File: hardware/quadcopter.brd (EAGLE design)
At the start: 130.1 x 130.1 mm, 91 parts, among them J1 HEADER-4POS-0.1IN-FEMALE-SMD-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, J2 HEADER-10POSTH-254X10, J3 HEADER-4POS-0.1IN-FEMALE, J4 AVR_SPI_PRG_6-SMD, M1 MOTOR_PADS_GND-MOLEX-SMD, M2 MOTOR_PADS_GND-MOLEX-SMD, M3 MOTOR_PADS_GND-MOLEX-SMD, M4 MOTOR_PADS_GND-MOLEX-SMD, P1 PROPELLOR-45MM, P2 PROPELLOR-45MM, P3 PROPELLOR-45MM, P4 PROPELLOR-45MM, Q1 N-MOSFET-SI2302DS, Q12 N-MOSFET-SI2302DS, Q2 N-MOSFET-SI2302DS, Q3 N-MOSFET-SI2302DS, Q4 N-MOSFET-SI2302DS, Q6 N-MOSFET-SI2302DS, Q8 N-MOSFET-SI2302DS, Q9 N-MOSFET-SI2302DS, SW1 PUSHBUTTON_-4.5X4.5, U1 ATMEGA128RFA1, U2 IMU_LSM9DS1-LSM9DS1, Y1 CRYSTAL5X3

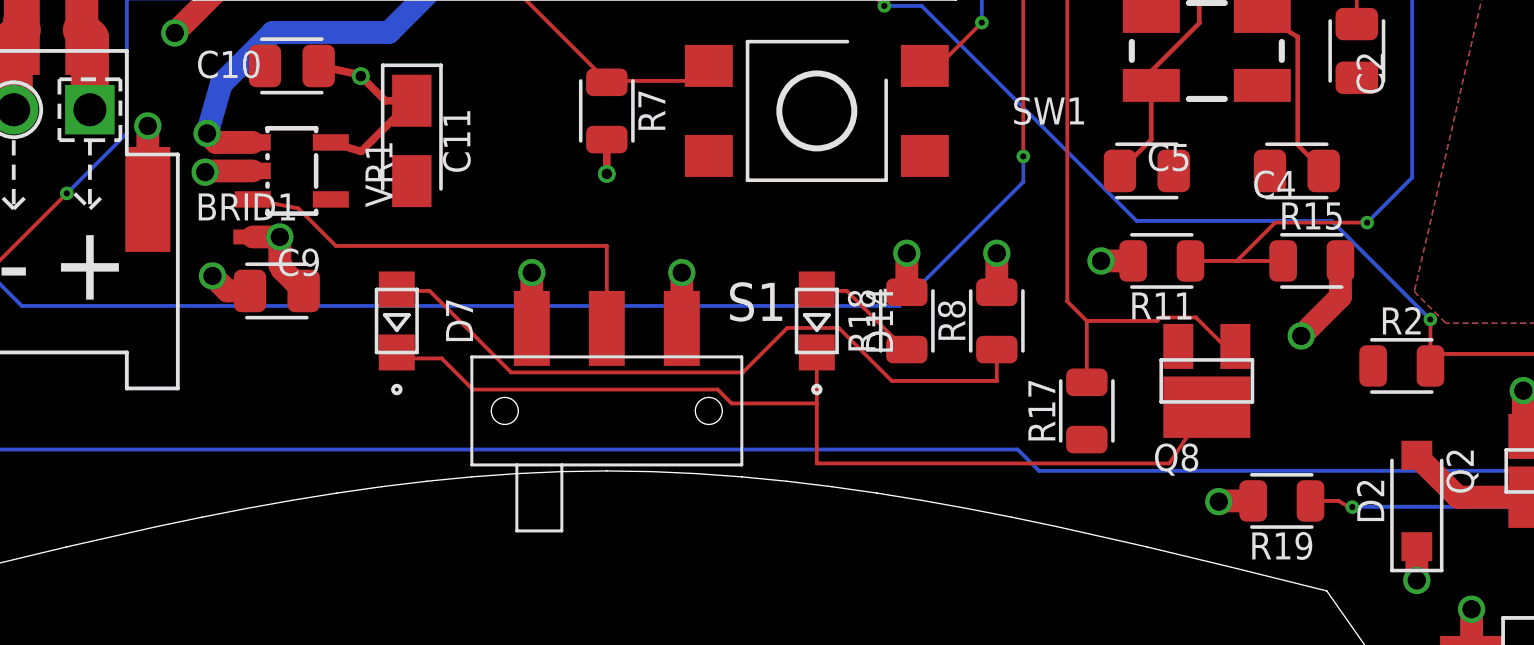
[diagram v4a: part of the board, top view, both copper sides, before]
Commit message: Aligned net bridge to 0.5mm grid
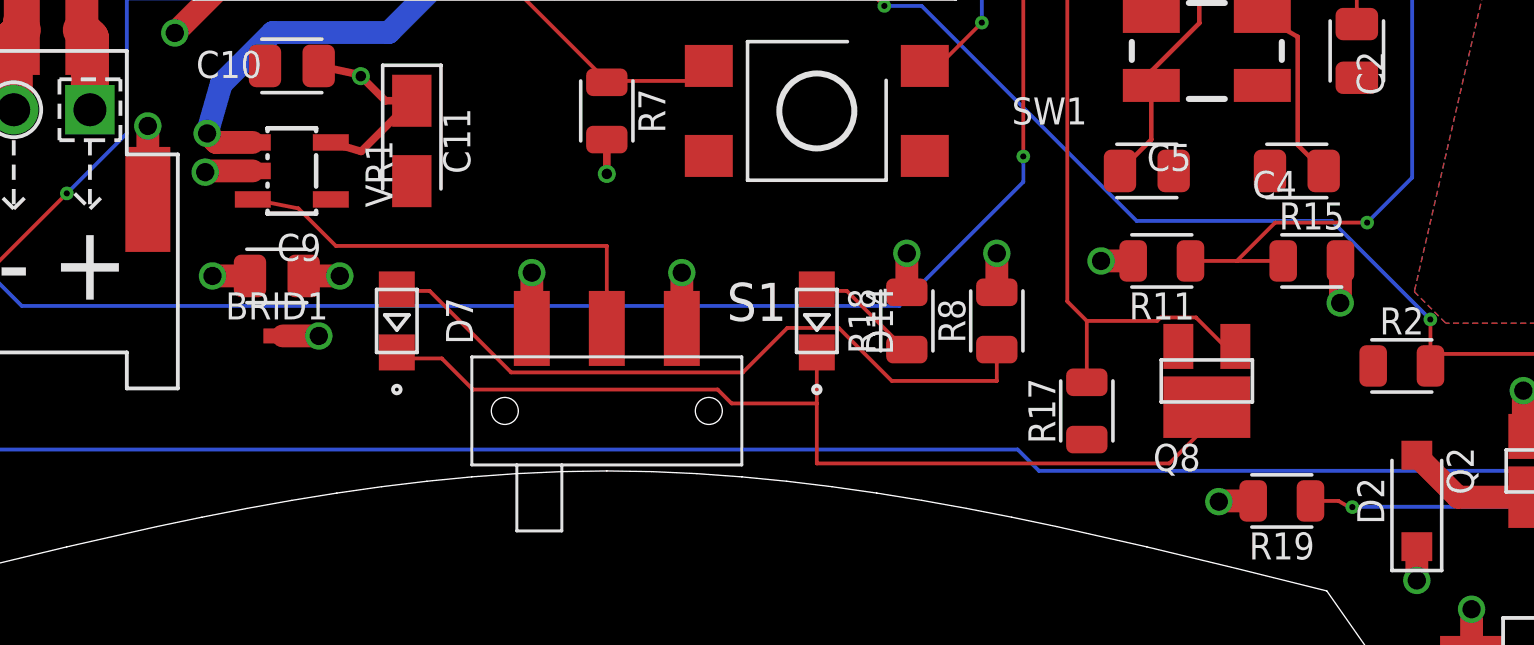
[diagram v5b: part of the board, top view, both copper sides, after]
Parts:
- moved BRID1 3.45 mm to (-11.0, -17.5)
- moved C9 0.50 mm to (-11.0, -15.5)
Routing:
- net BAT_GND: track 50.5 -> 48.2 mm, vias 21 -> 22
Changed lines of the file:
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@@
 <attribute name="NAME" x="-18.5" y="-4.5" size="0.9" layer="25" font="vector" align="center"/>
 </element>
-<element name="BRID1" library="custom_michael_shao" library_urn="urn:adsk.wipprod:fs.file:vf.WEX53KctTd223gU3vuBSuw" package="NET_BRIDGE_5X5" value="NET_BRIDGE_5X5" x="-12" y="-14.2" smashed="yes" rot="R180">
-<attribute name="CREATOR" value="Michael Shao" x="-37.4" y="83.59" size="1.778" layer="27" rot="R180" display="off"/>
-<attribute name="DIST" value="N/A" x="-37.4" y="83.59" size="1.778" layer="27" rot="R180" display="off"/>
-<attribute name="DISTPN" value="N/A" x="-37.4" y="83.59" size="1.778" layer="27" rot="R180" display="off"/>
-<attribute name="NAME" x="-12" y="-13.2" size="0.9" layer="25" font="vector" rot="R180" align="center"/>
+<element name="BRID1" library="custom_michael_shao" library_urn="urn:adsk.wipprod:fs.file:vf.WEX53KctTd223gU3vuBSuw" package="NET_BRIDGE_5X5" value="NET_BRIDGE_5X5" x="-11" y="-17.5" smashed="yes" rot="R180">
+<attribute name="CREATOR" value="Michael Shao" x="-36.4" y="80.29" size="1.778" layer="27" rot="R180" display="off"/>
+<attribute name="DIST" value="N/A" x="-36.4" y="80.29" size="1.778" layer="27" rot="R180" display="off"/>
+<attribute name="DISTPN" value="N/A" x="-36.4" y="80.29" size="1.778" layer="27" rot="R180" display="off"/>
+<attribute name="NAME" x="-11" y="-16.5" size="0.9" layer="25" font="vector" rot="R180" align="center"/>
 </element>
 <element name="C1" library="quadparts_prebuilt_2022" library_urn="urn:adsk.wipprod:fs.file:vf.VudH_-qgS-enOFMGlZoxrw" package="CAPC2012X140_HS" value="22pF" x="28" y="6.5" smashed="yes" rot="R270">
@@
 <attribute name="VALUE" x="20" y="11" size="0.9" layer="27" font="vector" rot="R90"/>
 </element>
-<element name="C9" library="quadparts_prebuilt_2022" library_urn="urn:adsk.wipprod:fs.file:vf.VudH_-qgS-enOFMGlZoxrw" package="CAPC2012X140_HS" value="1uF" x="-11" y="-16" smashed="yes">
-<attribute name="CREATOR" value="Swanson" x="4.24" y="-113.79" size="1.778" layer="27" display="off"/>
-<attribute name="DIST" value="Digikey" x="4.24" y="-113.79" size="1.778" layer="27" display="off"/>
-<attribute name="DISTPN" value="587-1281-1-ND" x="4.24" y="-113.79" size="1.778" layer="27" display="off"/>
-<attribute name="MFR" value="Taiyo Yuden" x="4.24" y="-113.79" size="1.778" layer="27" display="off"/>
-<attribute name="MOUNTING" value="SMD" x="4.24" y="-113.79" size="1.778" layer="27" display="off"/>
-<attribute name="MPN" value="TMK212B7105KG-T" x="4.24" y="-113.79" size="1.778" layer="27" display="off"/>
-<attribute name="NAME" x="-11" y="-15.5" size="0.9" layer="25" font="vector"/>
-<attribute name="REVIEWER" value="Swanson" x="4.24" y="-113.79" size="1.778" layer="27" display="off"/>
-<attribute name="VALUE" x="-10" y="-18" size="0.9" layer="27" font="vector"/>
+<element name="C9" library="quadparts_prebuilt_2022" library_urn="urn:adsk.wipprod:fs.file:vf.VudH_-qgS-enOFMGlZoxrw" package="CAPC2012X140_HS" value="1uF" x="-11" y="-15.5" smashed="yes">
+<attribute name="CREATOR" value="Swanson" x="4.24" y="-113.29" size="1.778" layer="27" display="off"/>
+<attribute name="DIST" value="Digikey" x="4.24" y="-113.29" size="1.778" layer="27" display="off"/>
+<attribute name="DISTPN" value="587-1281-1-ND" x="4.24" y="-113.29" size="1.778" layer="27" display="off"/>
+<attribute name="MFR" value="Taiyo Yuden" x="4.24" y="-113.29" size="1.778" layer="27" display="off"/>
+<attribute name="MOUNTING" value="SMD" x="4.24" y="-113.29" size="1.778" layer="27" display="off"/>
+<attribute name="MPN" value="TMK212B7105KG-T" x="4.24" y="-113.29" size="1.778" layer="27" display="off"/>
+<attribute name="NAME" x="-11" y="-15" size="0.9" layer="25" font="vector"/>
+<attribute name="REVIEWER" value="Swanson" x="4.24" y="-113.29" size="1.778" layer="27" display="off"/>
+<attribute name="VALUE" x="-10" y="-17.5" size="0.9" layer="27" font="vector"/>
 </element>
 <element name="D1" library="quadparts_prebuilt_2022" library_urn="urn:adsk.wipprod:fs.file:vf.VudH_-qgS-enOFMGlZoxrw" package="SODFL3516X96" package3d_urn="urn:adsk.eagle:package:11793366/1" value="360mV" x="32" y="22.5" smashed="yes" rot="R180">
@@
 <vertex x="14.98484375" y="14.0762"/>
 </polygon>
-<via x="23.1454" y="-17.5" extent="1-16" drill="0.6096"/>
+<via x="24.4454" y="-16.4" extent="1-16" drill="0.6096"/>
 <wire x1="-12.5" y1="-5" x2="-12.5" y2="-5.5" width="0.762" layer="1"/>
 <wire x1="-12.5" y1="-5.5" x2="-14.4" y2="-7.4" width="0.762" layer="1"/>
@@
 <wire x1="-21.7" y1="-12.95" x2="-21.7" y2="-10.5" width="0.762" layer="1"/>
 <via x="-21.7" y="-10.5" extent="1-16" drill="0.6096"/>
-<wire x1="24.455" y1="-15" x2="24.455" y2="-16.1904" width="0.762" layer="1"/>
-<wire x1="24.455" y1="-16.1904" x2="23.1454" y2="-17.5" width="0.762" layer="1"/>
+<wire x1="24.455" y1="-15" x2="24.455" y2="-16.3904" width="0.762" layer="1"/>
+<wire x1="24.455" y1="-16.3904" x2="24.4454" y2="-16.4" width="0.762" layer="1"/>
 <wire x1="-19.77" y1="-9.96" x2="-19.77" y2="-7.57" width="1.27" layer="1"/>
 <wire x1="-19.77" y1="-7.57" x2="-19.5" y2="-7.3" width="1.27" layer="1"/>
@@
 <wire x1="-13.3877125" y1="-12.0406" x2="-13.3471125" y2="-12" width="0.762" layer="1"/>
 <wire x1="-13.3471125" y1="-12" x2="-11.8" y2="-12" width="0.762" layer="1"/>
-<wire x1="-11.8" y1="-14.2" x2="-10.9" y2="-14.2" width="0.762" layer="1"/>
-<via x="-10.9" y="-14.2" extent="1-16" drill="0.6096"/>
-<wire x1="-10.105" y1="-16" x2="-10.8216" y2="-15.2834" width="0.762" layer="1"/>
-<wire x1="-10.8216" y1="-15.2834" x2="-10.8216" y2="-15.21456875" width="0.762" layer="1"/>
-<wire x1="-10.8216" y1="-15.21456875" x2="-10.9" y2="-15.13616875" width="0.762" layer="1"/>
-<wire x1="-10.9" y1="-15.13616875" x2="-10.9" y2="-14.2" width="0.762" layer="1"/>
+<via x="-9.6" y="-17.5" extent="1-16" drill="0.6096"/>
+<wire x1="-8.9" y1="-15.5" x2="-10.105" y2="-15.5" width="0.762" layer="1"/>
+<via x="-8.9" y="-15.5" extent="1-16" drill="0.6096"/>
+<wire x1="-10.8" y1="-17.5" x2="-9.6" y2="-17.5" width="0.762" layer="1"/>
 </signal>
 <signal name="VBAT" class="3">
@@
 <wire x1="-11.8" y1="-11.05" x2="-13.0245" y2="-11.05" width="0.762" layer="1"/>
 <wire x1="-13.0245" y1="-11.05" x2="-13.3245" y2="-10.75" width="0.762" layer="1"/>
-<wire x1="-11.895" y1="-16" x2="-12.6446" y2="-16" width="0.762" layer="1"/>
-<wire x1="-12.6446" y1="-16" x2="-13.1446" y2="-15.5" width="0.762" layer="1"/>
+<wire x1="-11.895" y1="-15.5" x2="-13.1446" y2="-15.5" width="0.762" layer="1"/>
 </signal>
 <signal name="N$1" class="3">
@@
 <wire x1="3.69554375" y1="-19.2865" x2="-4.4635" y2="-19.2865" width="0.127" layer="1"/>
 <wire x1="7" y1="-21.75" x2="18.75" y2="-21.75" width="0.127" layer="1"/>
-<wire x1="18.75" y1="-21.75" x2="20" y2="-19.875" width="0.127" layer="1"/>
+<wire x1="20" y1="-19.875" x2="20" y2="-20.5" width="0.127" layer="1"/>
+<wire x1="20" y1="-20.5" x2="18.75" y2="-21.75" width="0.127" layer="1"/>
 </signal>
 <signal name="N$28">

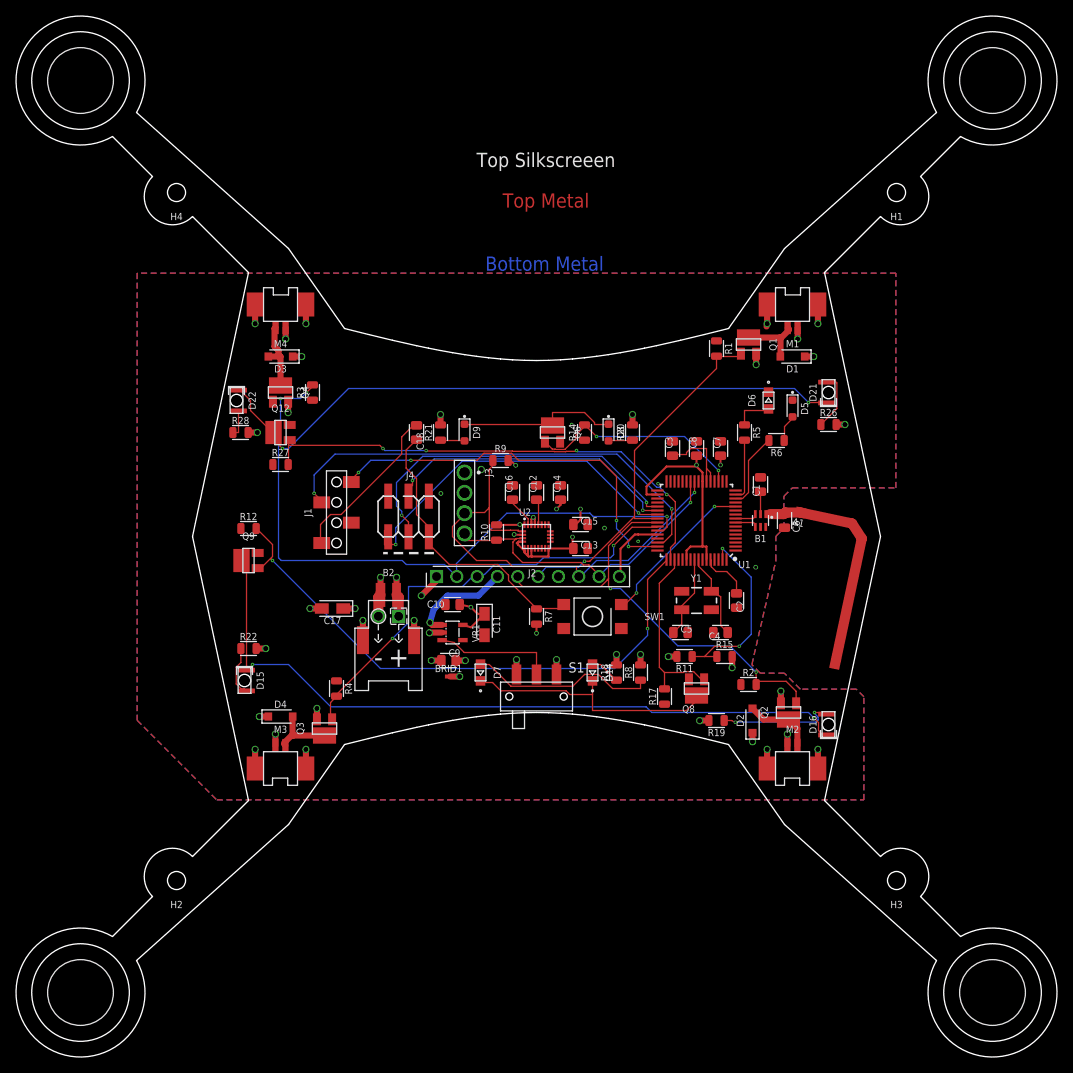
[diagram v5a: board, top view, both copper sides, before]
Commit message: Fixed issues identified in human review
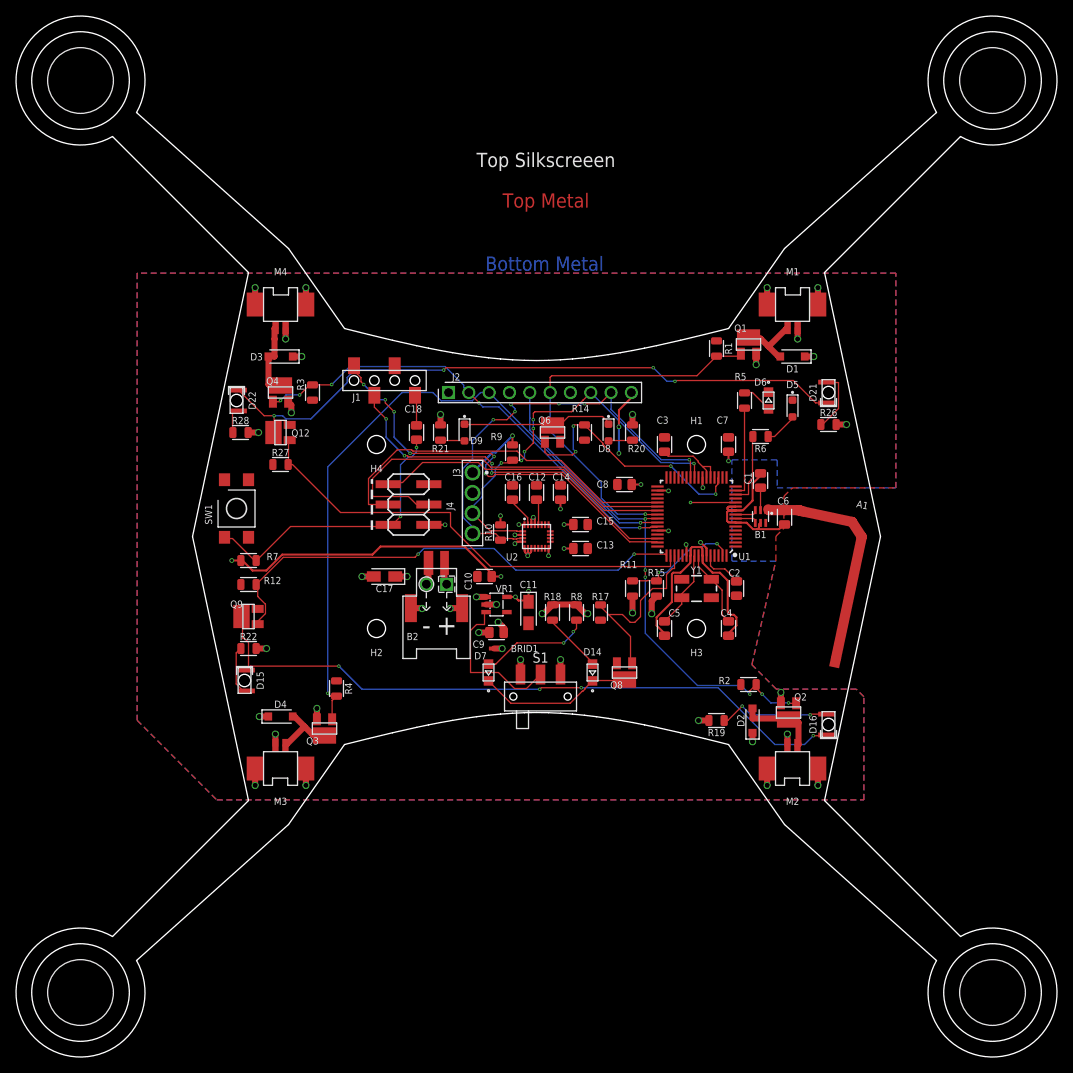
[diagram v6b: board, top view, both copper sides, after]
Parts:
- moved SW1 46.5 mm to (-37.5, 3.50), turned to 270 degrees
- moved H1 40.2 mm to (20.0, 11.5)
- moved H2 40.2 mm to (-20.0, -11.5)
- moved H3 40.2 mm to (20.0, -11.5)
- moved H4 40.2 mm to (-20.0, 11.5)
- moved R7 36.7 mm to (-36.0, -3.00), turned to 180 degrees
- moved J2 23.0 mm to (-11.0, 18.0)
- moved J1 17.6 mm to (-19.0, 19.5), turned to 180 degrees
- moved R17 13.2 mm to (8.00, -9.50)
- moved R15 12.0 mm to (15.0, -6.50), turned to 270 degrees
- moved R18 11.0 mm to (2.00, -9.50)
- moved R8 11.0 mm to (5.00, -9.50)
- moved R11 10.7 mm to (12.0, -6.50), turned to 270 degrees
- moved C8 10.1 mm to (11.0, 6.50), turned to 180 degrees
- moved Q8 9.22 mm to (11.0, -17.0)
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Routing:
- net GND: track 0.00 -> 50.8 mm, vias 7 -> 1
- net PWM3: track 55.7 -> 85.4 mm
- net PWM4: track 82.8 -> 58.5 mm, vias 3 -> 5
- net RESET: track 57.1 -> 79.5 mm, vias 2 -> 3
- net SDA: track 40.2 -> 57.3 mm, vias 1 -> 6
- net N$6: track 20.8 -> 3.85 mm
- net N$27: track 32.7 -> 19.5 mm
- net RX0: track 57.8 -> 45.8 mm, vias 2 -> 4
- net MOSI: track 37.3 -> 48.8 mm, vias 2 -> 0
- net 2V5: track 70.2 -> 81.4 mm, vias 11 -> 24
- net PWM5: track 71.9 -> 61.0 mm
- net BAT_GND: track 48.2 -> 37.9 mm, vias 22 -> 20
- net N$21: track 23.6 -> 14.0 mm, vias 0 -> 2
- net N$28: track 23.7 -> 14.9 mm
- net VBAT: track 44.0 -> 35.4 mm, vias 22 -> 21
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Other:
- outline, holes or cut-outs redrawn

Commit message: Moved wires around near pwr switch so that throughhole touched gnd
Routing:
- net N$27: track 19.5 -> 18.0 mm
- net N$35: track 85.0 -> 85.2 mm, vias 4 -> 2
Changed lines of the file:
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@@
 <setting verticaltext="up"/>
 </settings>
-<grid distance="0.5" unitdist="mm" unit="mm" style="lines" multiple="1" display="yes" altdistance="0.5" altunitdist="mm" altunit="mm"/>
+<grid distance="0.1" unitdist="mm" unit="mm" style="lines" multiple="1" display="yes" altdistance="0.5" altunitdist="mm" altunit="mm"/>
 <layers>
 <layer number="1" name="Top" color="4" fill="1" visible="yes" active="yes"/>
@@
 <via x="26.6654" y="-19.7" extent="1-16" drill="0.2032"/>
 <wire x1="26.6654" y1="-19.2896" x2="26.6654" y2="-19.7" width="0.127" layer="1"/>
-<wire x1="20.1206" y1="-18.6206" x2="13.6" y2="-12.1" width="0.127" layer="16"/>
-<wire x1="26.6654" y1="-19.7" x2="25.586" y2="-18.6206" width="0.127" layer="16"/>
-<wire x1="25.586" y1="-18.6206" x2="20.1206" y2="-18.6206" width="0.127" layer="16"/>
+<wire x1="19.6206" y1="-18.1206" x2="13.6" y2="-12.1" width="0.127" layer="16"/>
+<wire x1="26.6654" y1="-19.7" x2="25.086" y2="-18.1206" width="0.127" layer="16"/>
+<wire x1="25.086" y1="-18.1206" x2="19.6206" y2="-18.1206" width="0.127" layer="16"/>
 </signal>
 <signal name="N$3" class="3">
@@
 <wire x1="-8.25" y1="-17" x2="-8.25" y2="-11.75" width="0.127" layer="1"/>
 <wire x1="-4.75" y1="-17" x2="-8.25" y2="-17" width="0.127" layer="1"/>
-<wire x1="-2.75" y1="-19" x2="-4.75" y2="-17" width="0.127" layer="1"/>
-<wire x1="-1.25" y1="-19" x2="-2.75" y2="-19" width="0.127" layer="1"/>
-<wire x1="0.5" y1="-17.25" x2="-1.25" y2="-19" width="0.127" layer="1"/>
 <wire x1="-6.5" y1="-9.5" x2="-6.3" y2="-9.45" width="0.127" layer="1"/>
+<wire x1="0.5" y1="-17.25" x2="-0.9571" y2="-18.7071" width="0.127" layer="1"/>
+<wire x1="-0.9571" y1="-18.7071" x2="-1.30176875" y2="-18.7071" width="0.127" layer="1"/>
+<wire x1="-1.30176875" y1="-18.7071" x2="-1.31056875" y2="-18.7159" width="0.127" layer="1"/>
+<wire x1="-1.31056875" y1="-18.7159" x2="-3.0341" y2="-18.7159" width="0.127" layer="1"/>
+<wire x1="-3.0341" y1="-18.7159" x2="-4.75" y2="-17" width="0.127" layer="1"/>
 </signal>
 <signal name="SDA">
@@
 <wire x1="34.6" y1="-24.9" x2="33.5" y2="-26" width="0.127" layer="16"/>
 <wire x1="33.5" y1="-26" x2="29.8" y2="-26" width="0.127" layer="16"/>
-<via x="5.6" y="-18.9" extent="1-16" drill="0.2032"/>
-<wire x1="5.6" y1="-18.9" x2="0.6" y2="-18.9" width="0.127" layer="1"/>
-<wire x1="0.6" y1="-18.9" x2="0.4" y2="-19.1" width="0.127" layer="1"/>
-<via x="0.4" y="-19.1" extent="1-16" drill="0.2032"/>
-<wire x1="0.4" y1="-19.1" x2="-21.8" y2="-19.1" width="0.127" layer="16"/>
-<wire x1="-21.8" y1="-19.1" x2="-24.7" y2="-16.2" width="0.127" layer="16"/>
 <via x="-24.7" y="-16.2" extent="1-16" drill="0.2032"/>
 <wire x1="-24.7" y1="-16.2" x2="-35.75" y2="-16.2" width="0.127" layer="1"/>
 <wire x1="-35.75" y1="-16.2" x2="-36.25" y2="-16.7" width="0.127" layer="1"/>
-<wire x1="22.7" y1="-18.9" x2="5.6" y2="-18.9" width="0.127" layer="16"/>
-<wire x1="29.8" y1="-26" x2="22.7" y2="-18.9" width="0.127" layer="16"/>
+<wire x1="22.2" y1="-18.4" x2="5.6" y2="-18.4" width="0.127" layer="16"/>
+<wire x1="29.8" y1="-26" x2="22.2" y2="-18.4" width="0.127" layer="16"/>
+<wire x1="-22.058" y1="-18.842" x2="5.158" y2="-18.842" width="0.127" layer="16"/>
+<wire x1="-22.058" y1="-18.842" x2="-24.7" y2="-16.2" width="0.127" layer="16"/>
+<wire x1="5.158" y1="-18.842" x2="5.6" y2="-18.4" width="0.127" layer="16"/>
 </signal>
 <signal name="N$40">
@@
 <wire x1="11" y1="-18" x2="11" y2="-17.875" width="0.127" layer="1"/>
 <wire x1="7" y1="-18" x2="7" y2="-18.05" width="0.127" layer="1"/>
-<wire x1="4.2088" y1="-20.8412" x2="-3.2088" y2="-20.8412" width="0.127" layer="1"/>
-<wire x1="-3.2088" y1="-20.8412" x2="-6" y2="-18.05" width="0.127" layer="1"/>
-<wire x1="7" y1="-18.05" x2="6.0445" y2="-19.0055" width="0.127" layer="1"/>
-<wire x1="6.0445" y1="-19.0055" x2="6.0445" y2="-19.08411875" width="0.127" layer="1"/>
-<wire x1="6.0445" y1="-19.08411875" x2="5.78411875" y2="-19.3445" width="0.127" layer="1"/>
-<wire x1="5.78411875" y1="-19.3445" x2="5.7055" y2="-19.3445" width="0.127" layer="1"/>
-<wire x1="5.7055" y1="-19.3445" x2="4.2088" y2="-20.8412" width="0.127" layer="1"/>
+<wire x1="-6" y1="-18.15" x2="-6" y2="-18.05" width="0.127" layer="1"/>
+<wire x1="6.0547" y1="-18.9953" x2="-5.1547" y2="-18.9953" width="0.127" layer="1"/>
+<wire x1="-5.1547" y1="-18.9953" x2="-6" y2="-18.15" width="0.127" layer="1"/>
+<wire x1="6.0547" y1="-18.9953" x2="7" y2="-18.05" width="0.127" layer="1"/>
 </signal>
 <signal name="N$28">
